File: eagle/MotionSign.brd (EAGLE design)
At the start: 85.9 x 47.6 mm, 76 parts, among them Q1 16MHZ, U1 ATMEGA328, U2 L7805CDT-TR, U3 NCS36000, U4 PIR, U5 WS2801, U6 SPX3819, U7 NJVMJD2955T4G, U8 TXB0108PWR, U9 LCD-HD4478020X4-4HOLES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

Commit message: Fix board issues
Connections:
- removed net E: U8.18
- net LCD_E: now also U8.18
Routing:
- net LCD_E: track 0.00 -> 18.8 mm, vias 0 -> 1
- net LCD_D7: track 11.1 -> 12.0 mm
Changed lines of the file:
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@@
 <?xml version="1.0" encoding="utf-8"?>
 <!DOCTYPE eagle SYSTEM "eagle.dtd">
-<eagle version="9.0.0">
+<eagle version="9.0.1">
 <drawing>
 <settings>
@@
 <text x="121.666" y="4.445" size="1.778" layer="26" rot="MR0">VCC: 9-12V</text>
 <text x="121.666" y="6.477" size="1.778" layer="26" rot="MR0">MAX: 1.5A</text>
-<text x="102.616" y="11.303" size="1.016" layer="52" rot="MR0" align="bottom-center">LEDS</text>
-<text x="86.36" y="11.557" size="1.016" layer="51" align="bottom-center">POT</text>
+<text x="104.648" y="11.303" size="1.016" layer="26" rot="MR0" align="bottom-center">LEDS</text>
+<text x="86.36" y="11.557" size="1.016" layer="25" align="bottom-center">POT</text>
 <text x="83.185" y="10.795" size="0.508" layer="21" align="bottom-center">VCC</text>
 <text x="85.217" y="10.795" size="0.508" layer="21" align="bottom-center">POT</text>
@@
 <via x="47.498" y="11.684" extent="1-16" drill="0.381"/>
 <via x="73.66" y="43.434" extent="1-16" drill="0.381"/>
-<via x="119.634" y="35.306" extent="1-16" drill="0.4"/>
+<via x="119.761" y="35.179" extent="1-16" drill="0.4"/>
 </signal>
 <signal name="AREF">
@@
 <wire x1="58.227" y1="38.608" x2="71.755" y2="38.608" width="0.508" layer="1"/>
 <wire x1="71.755" y1="38.608" x2="73.787" y2="36.576" width="0.508" layer="1"/>
-<wire x1="56.576" y1="41.91" x2="58.38191875" y2="41.91" width="0.508" layer="1"/>
-<wire x1="58.38191875" y1="41.91" x2="59.193" y2="41.09891875" width="0.508" layer="1"/>
+<wire x1="56.576" y1="41.91" x2="58.38191875" y2="41.91" width="0.381" layer="1"/>
+<wire x1="58.38191875" y1="41.91" x2="59.193" y2="41.09891875" width="0.381" layer="1"/>
 <wire x1="59.193" y1="41.09891875" x2="59.182" y2="41.08791875" width="0.381" layer="1"/>
 <wire x1="59.182" y1="41.08791875" x2="59.182" y2="40.386" width="0.381" layer="1"/>
@@
 <wire x1="63.754" y1="40.386" x2="63.743" y2="40.3828" width="0.254" layer="1"/>
 <wire x1="90.805" y1="35.052" x2="90.8095375" y2="35.1491125" width="0.254" layer="1"/>
+<via x="87.122" y="35.814" extent="1-16" drill="0.381"/>
 <via x="78.232" y="42.164" extent="1-16" drill="0.381"/>
-<via x="87.122" y="35.814" extent="1-16" drill="0.381"/>
 </signal>
 <signal name="N$3">
@@
 <wire x1="78.994" y1="48.006" x2="78.9" y2="48.102" width="0.254" layer="1"/>
 </signal>
-<signal name="E">
-<contactref element="U8" pad="18"/>
-</signal>
 <signal name="LCD_D4">
 <contactref element="U9" pad="P$11"/>
@@
 <contactref element="U9" pad="P$14"/>
 <contactref element="U8" pad="17"/>
-<wire x1="60.452" y1="41.91" x2="60.452" y2="40.386" width="0.254" layer="1"/>
-<wire x1="54.356" y1="48.006" x2="60.452" y2="41.91" width="0.254" layer="1"/>
-<wire x1="53.594" y1="48.006" x2="54.356" y2="48.006" width="0.254" layer="1"/>
-<wire x1="60.452" y1="40.386" x2="60.493" y2="40.3828" width="0.254" layer="1"/>
-<wire x1="53.594" y1="48.006" x2="53.5" y2="48.102" width="0.254" layer="1"/>
+<wire x1="60.493" y1="40.3828" x2="60.452" y2="40.386" width="0.254" layer="1"/>
+<wire x1="60.452" y1="42.926" x2="56.642" y2="46.736" width="0.254" layer="1"/>
+<wire x1="56.642" y1="46.736" x2="54.356" y2="46.736" width="0.254" layer="1"/>
+<wire x1="54.356" y1="46.736" x2="53.5" y2="47.592" width="0.254" layer="1"/>
+<wire x1="53.5" y1="47.592" x2="53.5" y2="48.102" width="0.254" layer="1"/>
+<wire x1="60.452" y1="40.386" x2="60.452" y2="42.926" width="0.254" layer="1"/>
 </signal>
 <signal name="LCD_D5">
@@
 <signal name="LCD_E">
 <contactref element="U9" pad="P$6"/>
+<contactref element="U8" pad="18"/>
+<wire x1="59.817" y1="40.894" x2="59.817" y2="40.386" width="0.254" layer="1"/>
+<wire x1="59.817" y1="40.386" x2="59.843" y2="40.3828" width="0.254" layer="1"/>
+<via x="59.69" y="41.91" extent="1-16" drill="0.381"/>
+<wire x1="59.843" y1="40.3828" x2="59.843" y2="41.757" width="0.254" layer="1"/>
+<wire x1="59.843" y1="41.757" x2="59.69" y2="41.91" width="0.254" layer="1"/>
+<wire x1="73.82" y1="48.102" x2="72.89645" y2="48.102" width="0.254" layer="16"/>
+<wire x1="64.739" y1="46.959" x2="59.69" y2="41.91" width="0.254" layer="16"/>
+<wire x1="72.89645" y1="48.102" x2="71.75345" y2="46.959" width="0.254" layer="16"/>
+<wire x1="71.75345" y1="46.959" x2="64.739" y2="46.959" width="0.254" layer="16"/>
 </signal>
 <signal name="N$17">

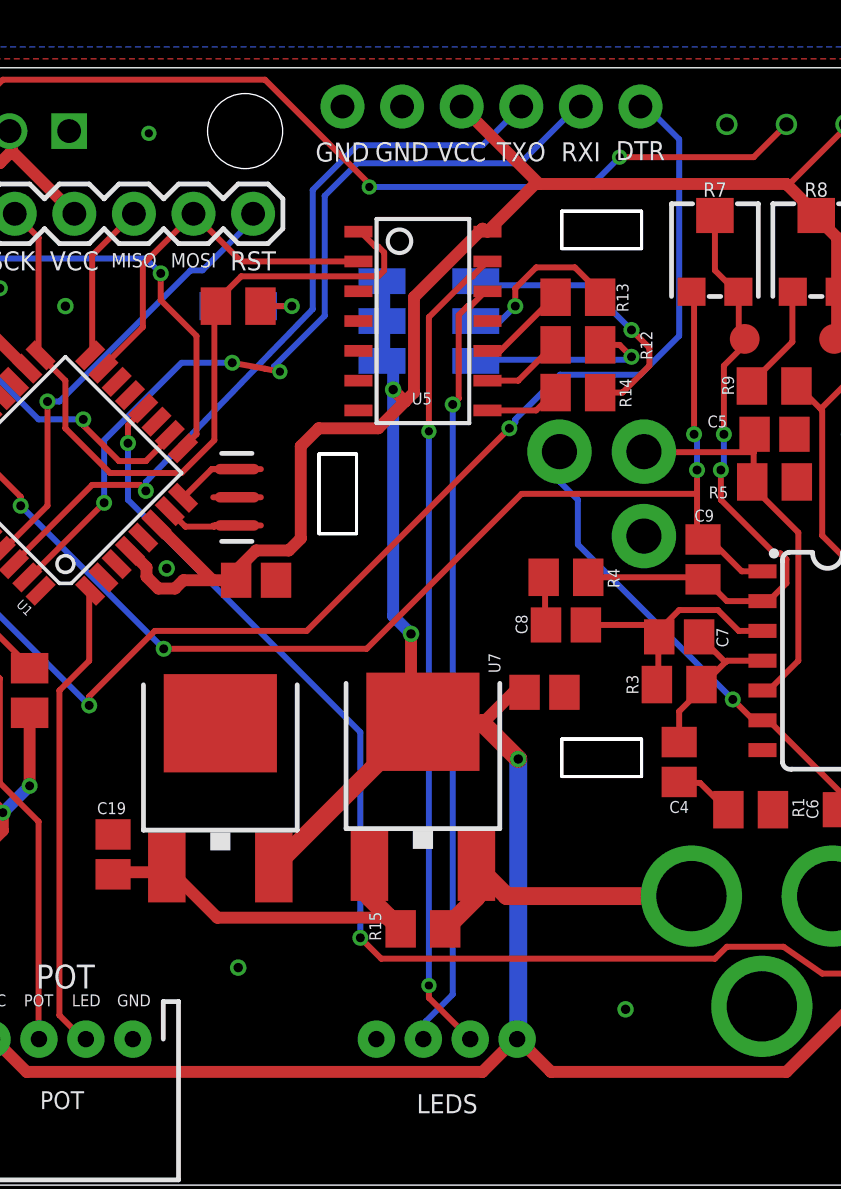
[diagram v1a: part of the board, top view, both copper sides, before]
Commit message: Add 5V jumper
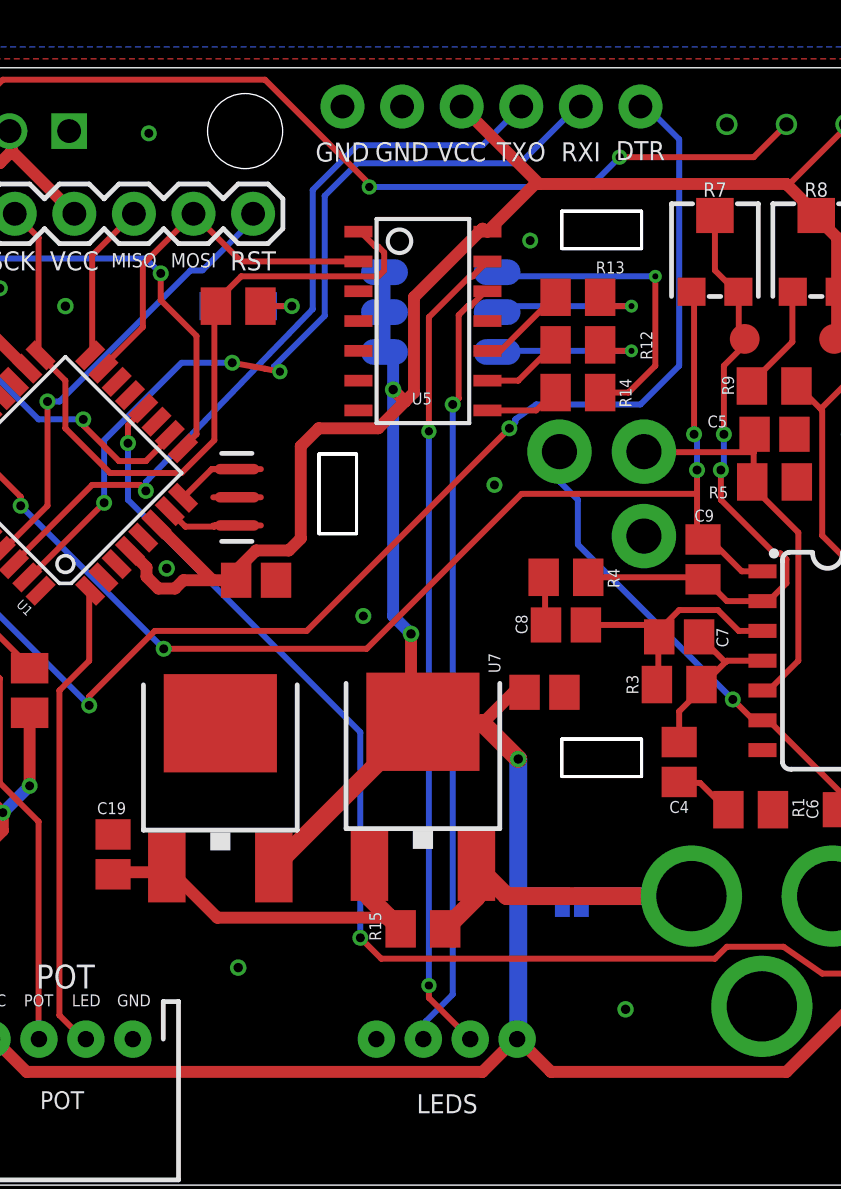
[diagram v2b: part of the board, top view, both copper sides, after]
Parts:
- removed LED2: RGBLED5050, adafruit:RGBLED5050
- added D6: (no value), SparkFun-LED:LED-TRICOLOR-5050
- added JP2: USE 5V POWER, SparkFun-Jumpers:SMT-JUMPER_2_NO_SILK
- C10: value 0.1uF -> 22uF
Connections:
- net N$20: now also D6.4; no longer LED2.4
- net N$21: now also D6.6; no longer LED2.6
- net N$22: now also D6.5; no longer LED2.5
- net RAW: now also JP2.1
- net VCC: now also D6.1, D6.2, D6.3, JP2.2; no longer LED2.1, LED2.2, LED2.3
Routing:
- net RAW: track 12.9 -> 17.7 mm
- net N$20: track 11.9 -> 14.1 mm
- net VCC: track 283.0 -> 285.0 mm
- net N$21: track 8.26 -> 7.30 mm
- net DTR: track 55.1 -> 55.8 mm
- net GND: vias 22 -> 26
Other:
- board text added: "<-InTentss=Designs-> ||-MotionSign V1-||"
- board text removed: "<-InTentss=Designs-> ||-MotionSign V0-||"

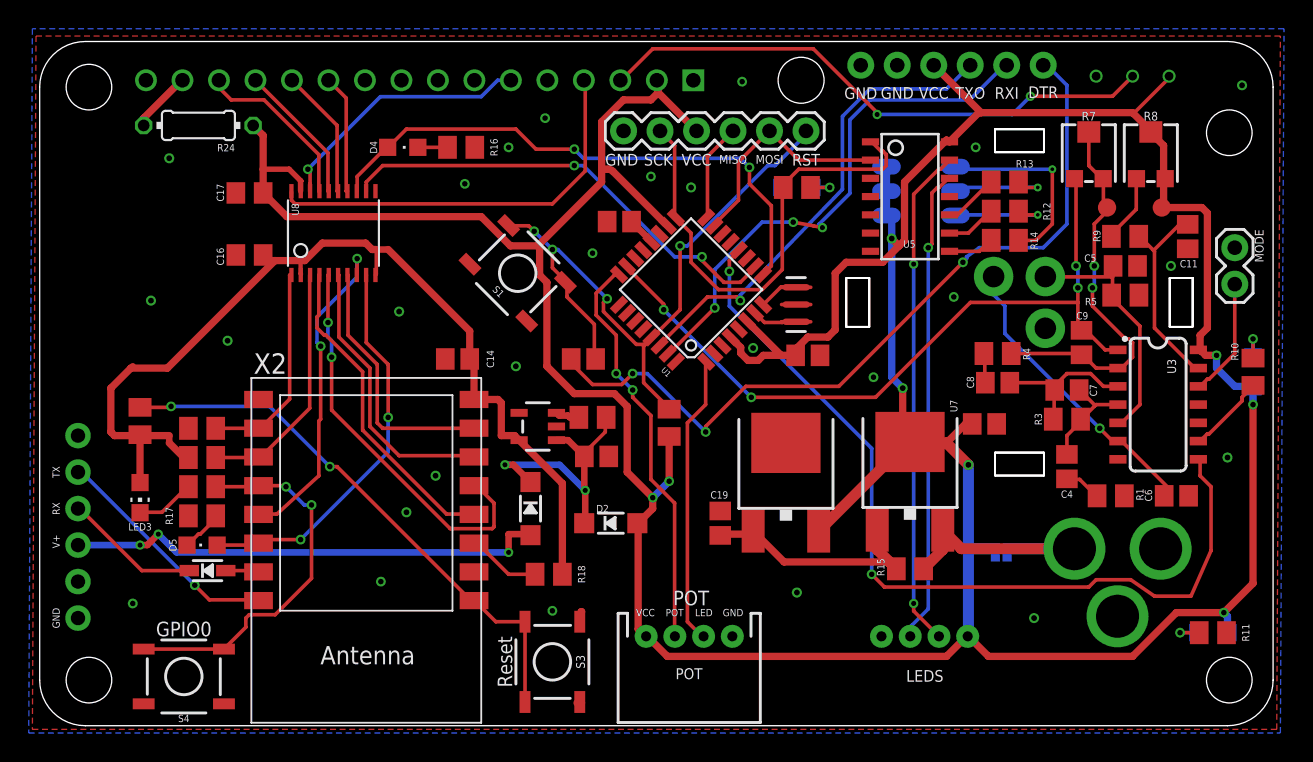
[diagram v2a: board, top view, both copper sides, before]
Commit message: Switch to Managed Libary for MotionSign
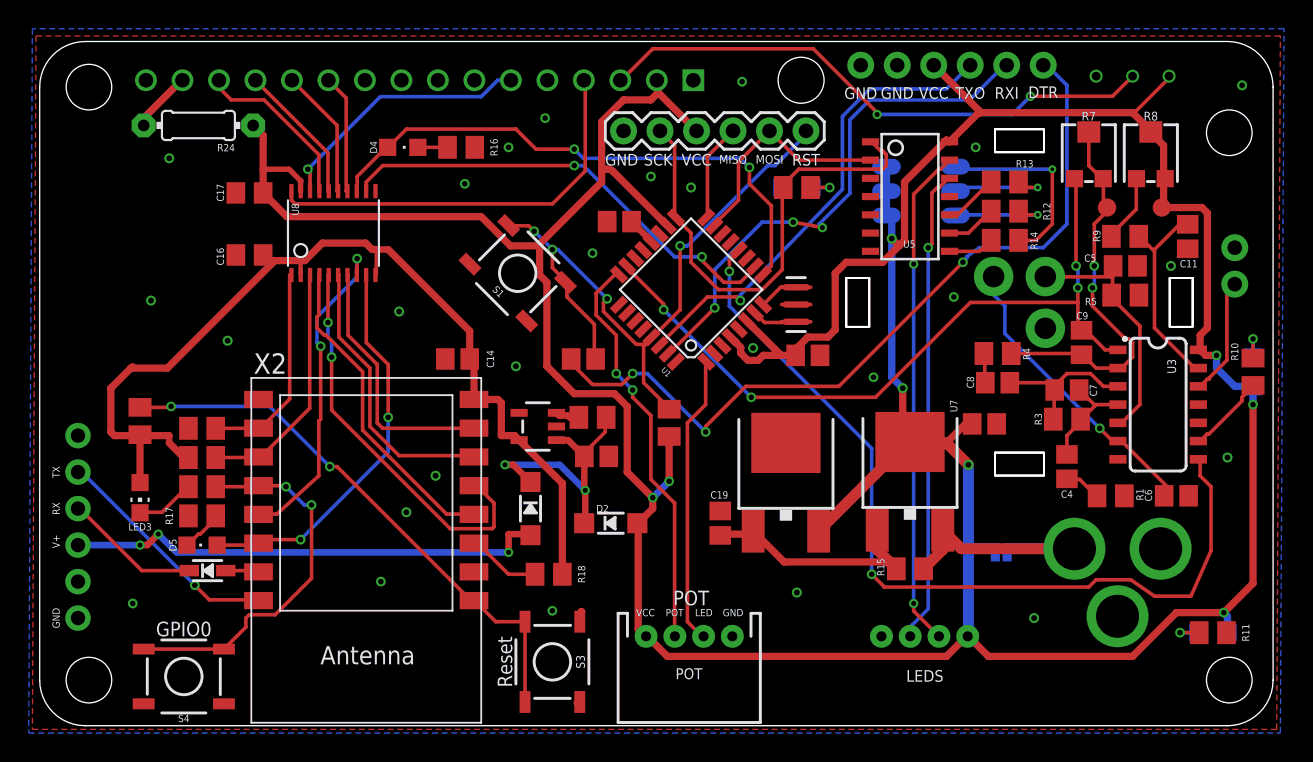
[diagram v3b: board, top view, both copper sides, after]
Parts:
- C1, C10, C11, C14, C15, C19, C2, C3, C4, C5, C6, C7, C8, C9: device adafruit:C0805 -> MotionSign:C0805
- CTRST: device resistor:RTRIM3296W -> MotionSign:RTRIM3296W
- D10, D2: device microbuilder:SOD-123 -> MotionSign:SOD-123
- D6: device SparkFun-LED:LED-TRICOLOR-5050 -> MotionSign:LED-TRICOLOR-5050
- D9: device microbuilder:SOD-323 -> MotionSign:SOD-323
- FRAME1: device SparkFun-Aesthetics:CREATIVE_COMMONS -> MotionSign:CREATIVE_COMMONS
- ISP_V13: device SparkFun-Connectors:1X06 -> MotionSign:1X06
- JP1: device SparkFun:1X06 -> MotionSign:1X06
- JP2: device SparkFun-Jumpers:SMT-JUMPER_2_NO_SILK -> MotionSign:SMT-JUMPER_2_NO_SILK
- JP4: device SparkFun-Connectors:POWER_JACK_PTH -> MotionSign:POWER_JACK_PTH
- JP6: device microbuilder:1X06_ROUND_70 -> MotionSign:1X06_ROUND_70
- LEDS, POT: device SparkFun-Connectors:JST-4-PTH -> MotionSign:JST-4-PTH
- MODE: device SparkFun-Connectors:1X02 -> MotionSign:1X02
- Q1: device SparkFun-FreqCtrl:RESONATOR-SMD -> MotionSign:RESONATOR-SMD
- R1, R10, R11, R12, R13, R14, R15, R16, R17, R18, R19, R2, R20, R21, R22, R23, R3, R4, R5, R6, R9: device adafruit:M0805 -> MotionSign:M0805
- R24: device resistor:0204/7 -> MotionSign:0204/7
- R7, R8: device openPIR-temp:TRIMPOT-TC33X -> MotionSign:TRIMPOT-TC33X
- S1, S3, S4: device SparkFun-Switches:TACTILE_SWITCH_SMD_5.2MM -> MotionSign:TACTILE_SWITCH_SMD_5.2MM
- TP1, TP2: value (none) -> TEST-POINT3X5; device SparkFun-Connectors:PAD.03X.05 -> MotionSign:PAD.03X.05
- U$1: device openPIR-temp:LENS-CWM-0.5-GI-V1 -> MotionSign:LENS-CWM-0.5-GI-V1
- U1: device SparkFun:TQFP32-08 -> MotionSign:TQFP32-08
- U2: device BAG:DPAK -> MotionSign:DPAK
- U3: device openPIR-temp:SO14 -> MotionSign:SO14
- U4: device openPIR-temp:PIR -> MotionSign:PIR
- U5: device SparkFun-DigitalIC:SOP-14 -> MotionSign:SOP-14
- U6: device microbuilder:SOT23-5 -> MotionSign:SOT23-5
- U7: device bg_eagle_lib:DPAK -> MotionSign:DPAK
- U8: device microbuilder:TSSOP20 -> MotionSign:TSSOP20
- U9: device HD44780LCD:LCD-20X4-1HOLE_NOSILK -> MotionSign:LCD-20X4-1HOLE_NOSILK
- X2: device microbuilder:ESP-12 -> MotionSign:ESP-12
- flipped MODE to the bottom
